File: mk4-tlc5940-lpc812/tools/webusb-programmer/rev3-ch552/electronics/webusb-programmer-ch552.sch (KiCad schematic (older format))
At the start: 19 parts, among them J1 Light Controller, J2 USB_B_Micro, U1 STMPS2141STR, U2 CH552G

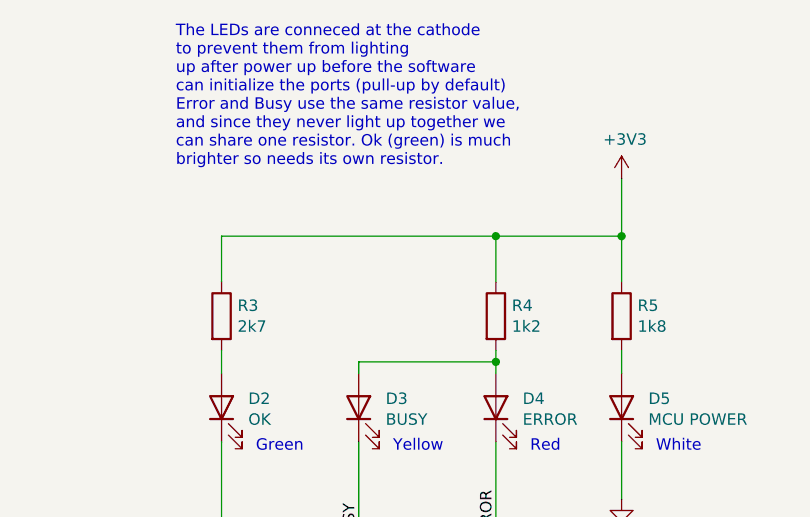
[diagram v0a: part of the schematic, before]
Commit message: Update schematics to reflect green LED being low brightness
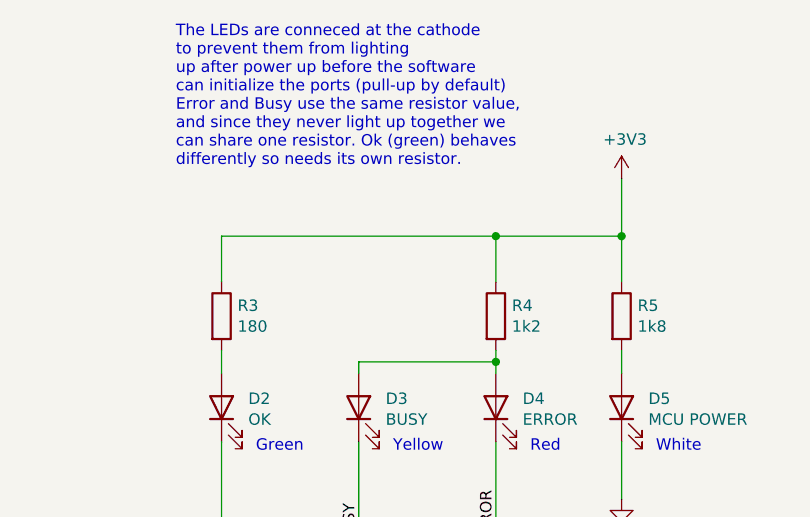
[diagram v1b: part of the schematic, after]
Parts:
- R3: value 2k7 -> 180
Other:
- note added: "The LEDs are conneced at the cathode\nto prevent them from lighting\nup after power up before the software\ncan initialize the ports (pull-up by default)\nError and Busy use the same resistor value, \nand since they never light up together we \ncan share one resistor. Ok (green) behaves\ndifferently so needs its own resistor."
- note removed: "The LEDs are conneced at the cathode\nto prevent them from lighting\nup after power up before the software\ncan initialize the ports (pull-up by default)\nError and Busy use the same resistor value, \nand since they never light up together we \ncan share one resistor. Ok (green) is much\nbrighter so needs its own resistor."
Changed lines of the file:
@@
 $EndComp
 Text Notes 3550 1400 0    50   ~ 0
-The LEDs are conneced at the cathode\nto prevent them from lighting\nup after power up before the software\ncan initialize the ports (pull-up by default)\nError and Busy use the same resistor value, \nand since they never light up together we \ncan share one resistor. Ok (green) is much\nbrighter so needs its own resistor.
+The LEDs are conneced at the cathode\nto prevent them from lighting\nup after power up before the software\ncan initialize the ports (pull-up by default)\nError and Busy use the same resistor value, \nand since they never light up together we \ncan share one resistor. Ok (green) behaves\ndifferently so needs its own resistor.
 $Comp
 L Connector:TestPoint TP1
@@
 P 3750 2050
 F 0 "R3" H 3820 2096 50  0000 L CNN
-F 1 "2k7" H 3820 2005 50  0000 L CNN
+F 1 "180" H 3820 2005 50  0000 L CNN
 F 2 "Resistor_SMD:R_0603_1608Metric_Pad1.05x0.95mm_HandSolder" V 3680 2050 50  0001 C CNN
 F 3 "~" H 3750 2050 50  0001 C CNN
